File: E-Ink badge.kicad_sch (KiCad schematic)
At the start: 16 parts, among them J1 USB_C_Receptacle_USB2.0_14P, J2 E-INK-FPC, Q1 BSS138, U1 RP2040, U2 AP2112K-3.3, Y1 Crystal

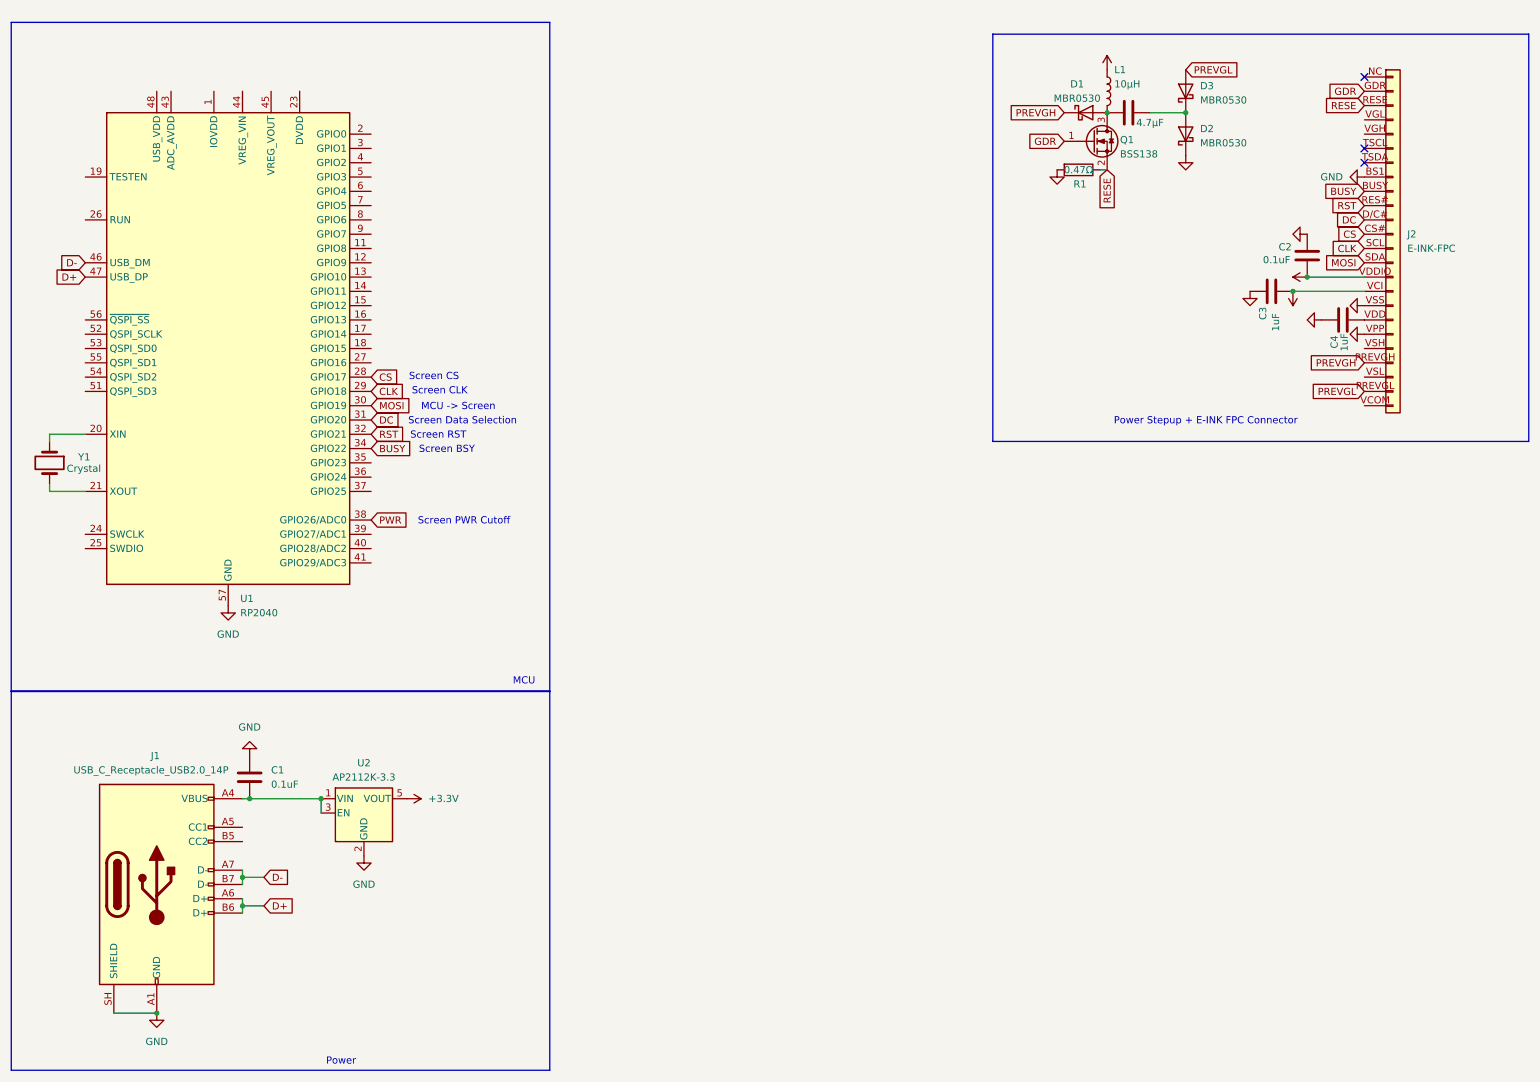
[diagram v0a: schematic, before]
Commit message: FPC + NAND Flash done
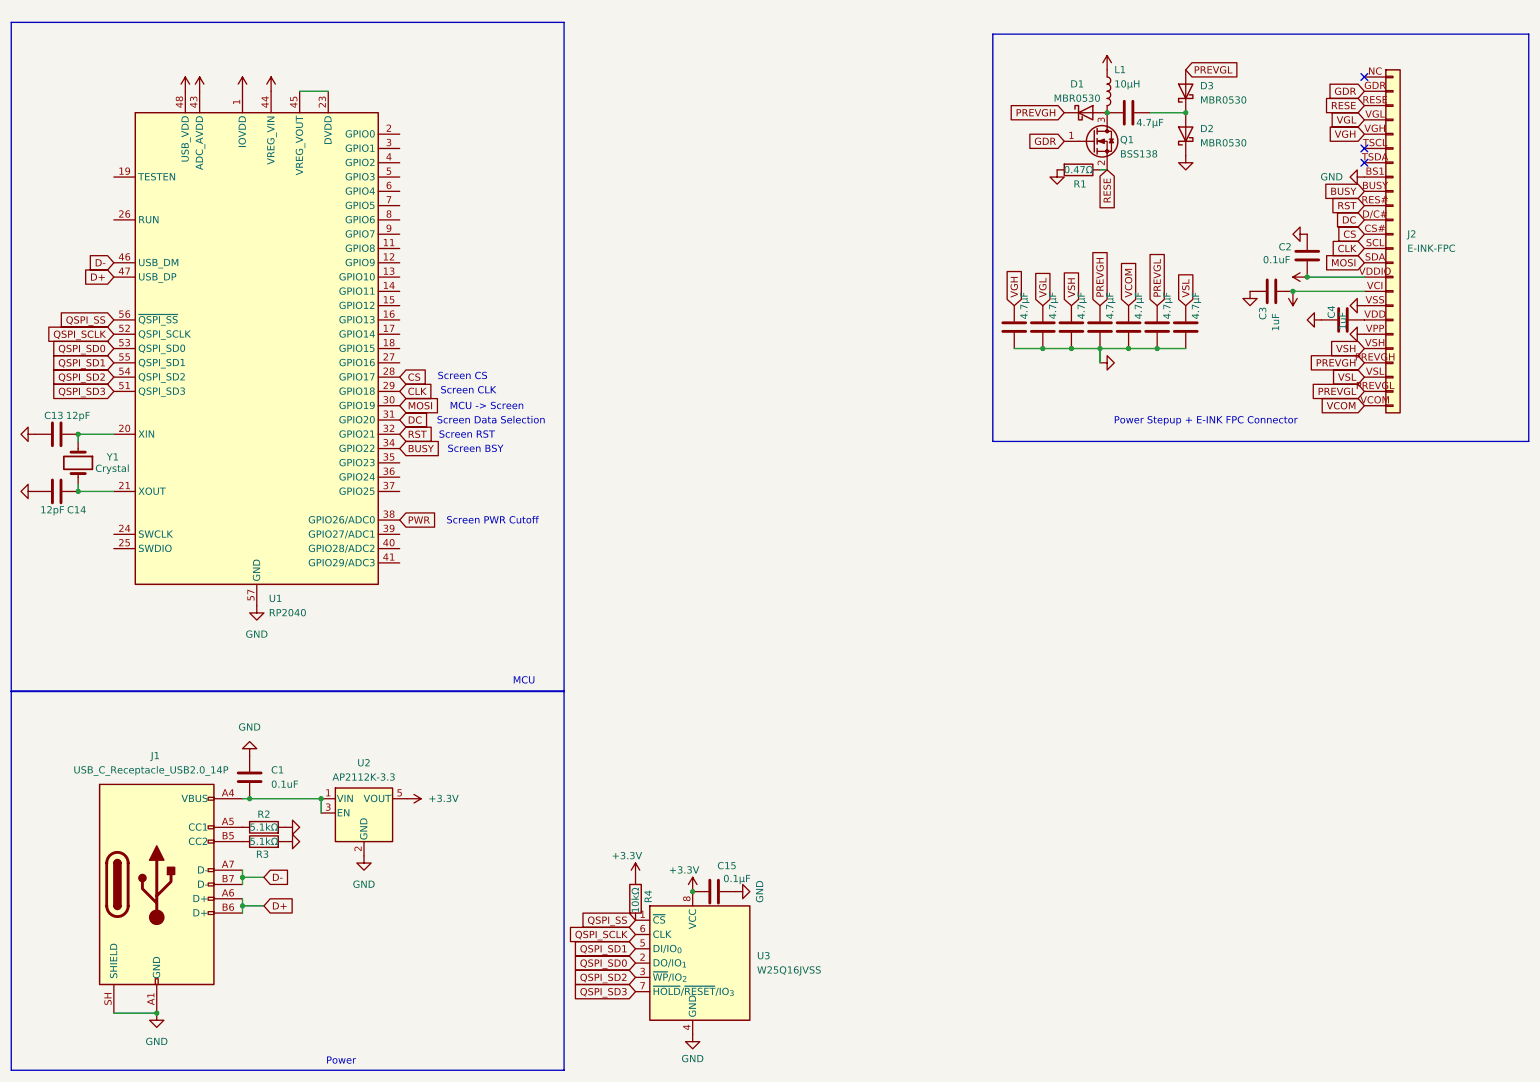
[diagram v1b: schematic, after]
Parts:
- added C10, C11, C12, C6, C7, C8, C9: 4.7µF, symbol Device:C
- added C13, C14: 12pF, Capacitor_SMD:C_0603_1608Metric, symbol Device:C
- added C15: 0.1µF, symbol Device:C
- added R2, R3: 5.1kΩ, symbol Device:R
- added R4: 10kΩ, symbol Device:R
- added U3: W25Q16JVSS, Package_SO:SOIC-8_5.3x5.3mm_P1.27mm, symbol Memory_Flash:W25Q16JVSS
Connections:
- net +3.3V: now also U1.1 (IOVDD), U1.10 (IOVDD), U1.22 (IOVDD), U1.33 (IOVDD), U1.42 (IOVDD), U1.43 (ADC_AVDD), U1.44 (VREG_VIN), U1.48 (USB_VDD), U1.49 (IOVDD), C15.1, R4.1, U3.8 (VCC)
- net GND: now also C10.1, C11.1, C12.1, C13.2, C14.2, C15.2, C6.1, C7.1, C8.1, C9.1, R2.2, R3.2, U3.4 (GND)
- net PREVGH: now also C9.2
- net PREVGL: now also C11.2
- net at U1.20 (XIN), Y1.1: now also C13.1
- net at U1.21 (XOUT), Y1.2: now also C14.1
- net at U1.23 (DVDD), U1.50 (DVDD): now also U1.45 (VREG_VOUT)
- net QSPI_SD3: now reaches U1.51 (QSPI_SD3)
- net QSPI_SD3: now also U3.7 (~{HOLD}/~{RESET}/IO_{3})
- net QSPI_SCLK: now reaches U1.52 (QSPI_SCLK)
- net QSPI_SCLK: now also U3.6 (CLK)
- net QSPI_SD0: now reaches U1.53 (QSPI_SD0)
- net QSPI_SD0: now also U3.2 (DO/IO_{1})
- net QSPI_SD2: now reaches U1.54 (QSPI_SD2)
- net QSPI_SD2: now also U3.3 (~{WP}/IO_{2})
- net QSPI_SD1: now reaches U1.55 (QSPI_SD1)
- net QSPI_SD1: now also U3.5 (DI/IO_{0})
- net QSPI_SS: now reaches U1.56 (~{QSPI_SS})
- net QSPI_SS: now also R4.2, U3.1 (~{CS})
- net VCOM: now reaches J2.VCOM (Pin_24)
- net VCOM: now also C10.2
- net VGH: now reaches J2.VGH (Pin_5)
- net VGH: now also C6.2
- net VGL: now reaches J2.VGL (Pin_4)
- net VGL: now also C7.2
- net VSH: now reaches J2.VSH (Pin_20)
- net VSH: now also C8.2
- net VSL: now reaches J2.VSL (Pin_22)
- net VSL: now also C12.2
- net at J1.A5 (CC1): now also R2.1
- net at J1.B5 (CC2): now also R3.1
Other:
- moved on the sheet: U1, Y1

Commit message: BOOTSEL + RUN wired up
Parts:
- added R5: 1kΩ, symbol Device:R
- added R6: 10kΩ, symbol Device:R
- added SW1: BOOTSEL, symbol Switch:SW_Push
- added SW2: RUN, symbol Switch:SW_Push
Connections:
- net +3.3V: now also R6.2
- net GND: now also U1.19 (TESTEN), SW1.1, SW2.1
- net RUN: now reaches U1.26 (RUN)
- net RUN: now also R6.1, SW2.2
- net QSPI_SS renamed BOOTSEL
- net BOOTSEL: now also R5.2
- new net: R5.1, SW1.2

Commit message: Finished the main schematic besides for some pwr cutoff stuff
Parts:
- added R7, R8: 27Ω, symbol Device:R
- added SW3: W, symbol Switch:SW_Push
- added SW4: A, symbol Switch:SW_Push
- added SW5: S, symbol Switch:SW_Push
- added SW6: D, symbol Switch:SW_Push
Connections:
- net D+: now also R8.2; no longer U1.47 (USB_DP)
- net D-: now also R7.1; no longer U1.46 (USB_DM)
- net GND: now also SW3.1, SW4.1, SW5.1, SW6.1
- net GPIO_W: now reaches U1.2 (GPIO0)
- net GPIO_W: now also SW3.2
- net GPIO_A: now reaches U1.3 (GPIO1)
- net GPIO_A: now also SW4.2
- net GPIO_S: now reaches U1.4 (GPIO2)
- net GPIO_S: now also SW5.2
- net GPIO_D: now reaches U1.5 (GPIO3)
- net GPIO_D: now also SW6.2
- new net: R7.2, U1.46 (USB_DM)
- new net: R8.1, U1.47 (USB_DP)

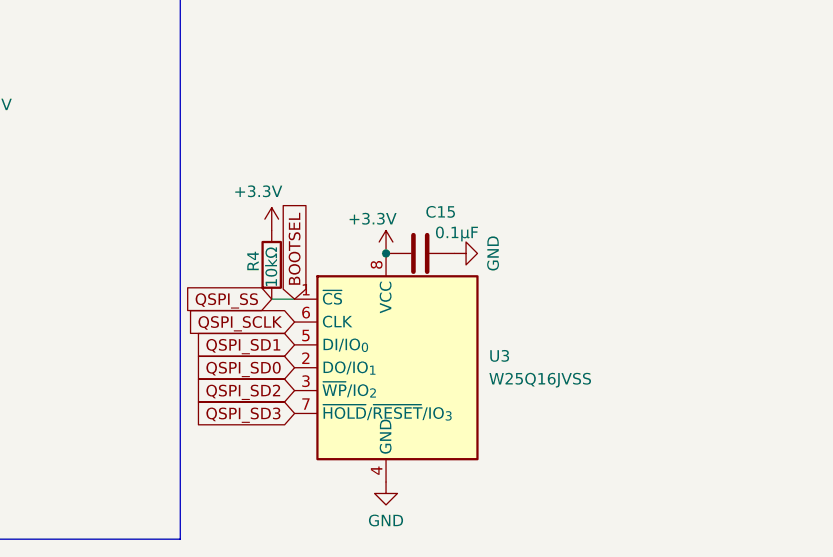
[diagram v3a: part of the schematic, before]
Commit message: Continued routing the PCB
routed parts of the MCU, most of the FPC Cable and stuff like that.
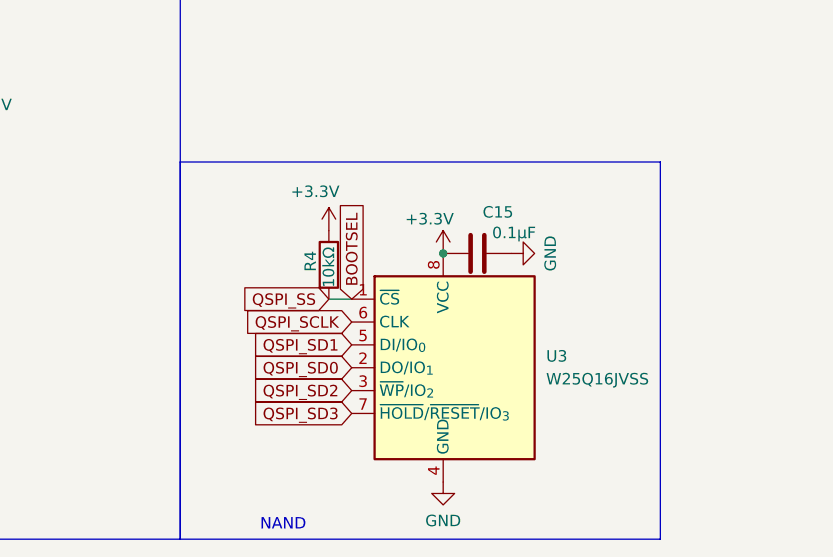
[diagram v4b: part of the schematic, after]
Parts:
- C1, C10, C11, C12, C15, C2, C3, C4, C5, C6, C7, C8, C9, R1, R2, R3, R4, R5, R6, R7, R8: footprint (none) -> Capacitor_SMD:C_0402_1005Metric
- C13, C14: footprint Capacitor_SMD:C_0603_1608Metric -> Capacitor_SMD:C_0402_1005Metric
- J1: footprint (none) -> Connector_USB:USB_C_Receptacle_GCT_USB4105-xx-A_16P_TopMnt_Horizontal
- L1: footprint (none) -> Inductor_SMD:L_0805_2012Metric
- SW1, SW2, SW3, SW4, SW5, SW6: footprint (none) -> Button_Switch_SMD:SW_SPST_PTS645Sx43SMTR92
- Y1: footprint (none) -> Crystal:Crystal_SMD_3215-2Pin_3.2x1.5mm
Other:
- note added: "NAND"
- moved on the sheet: C15, R4, U3

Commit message: Finally finished routing the whole board!
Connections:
- net GPIO_A: now also U1.12 (GPIO9); no longer U1.3 (GPIO1)
- net GPIO_D: now also U1.13 (GPIO10); no longer U1.5 (GPIO3)
- net GPIO_S: now also U1.14 (GPIO11); no longer U1.4 (GPIO2)
- net GPIO_W: now also U1.11 (GPIO8); no longer U1.2 (GPIO0)
